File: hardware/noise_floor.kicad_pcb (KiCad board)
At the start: 2 copper layers, 51.5 x 61.6 mm, 15 parts, among them J1 DC Power, J10 IO/Switch Connector 2 (Switch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, J2 Input, J3 Output, J4 Battery Negative (optional), J5 Battery Positive (optional), J6 IO/Effect Connector 1 (IO Sid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, J7 IO/Switch Connector 1 (IO Sid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, J8 IO/Switch Connector 2 (IO Sid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, J9 IO/Switch Connector 1 (Switch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, SW1 Footswitch

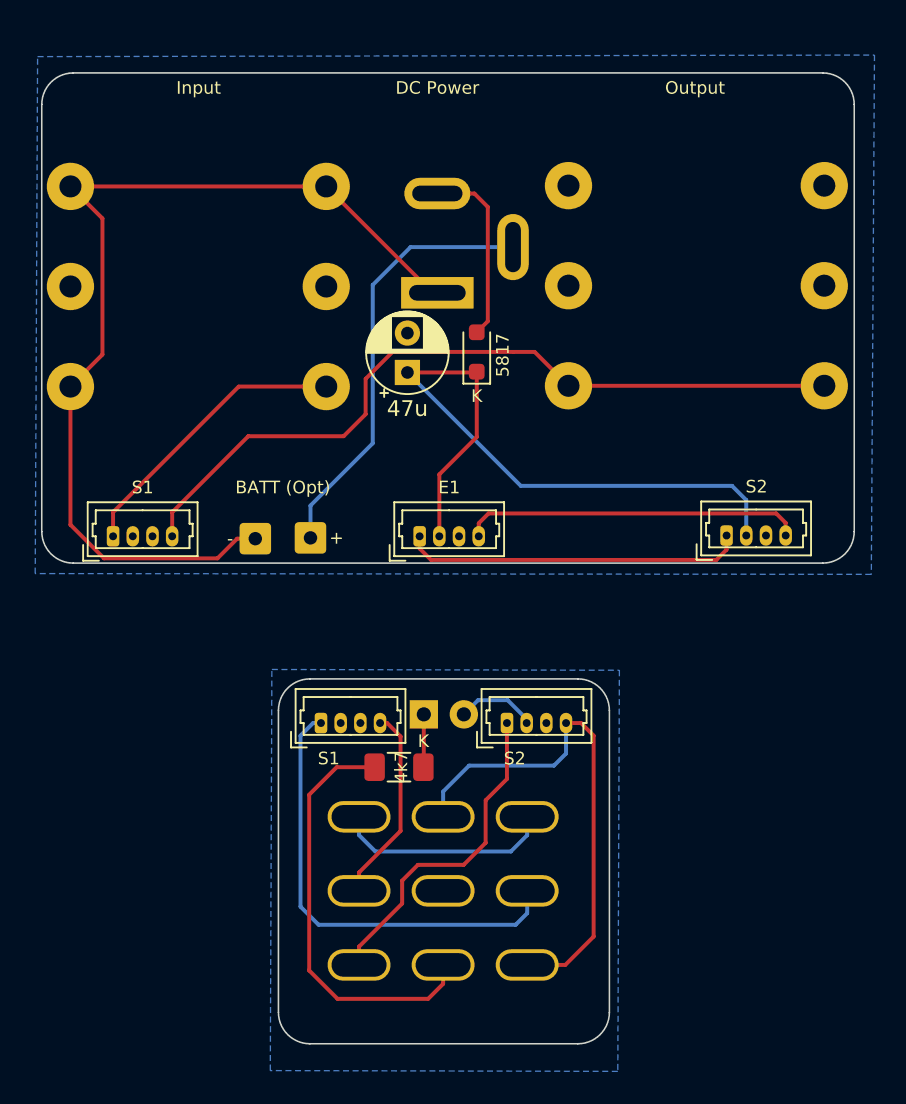
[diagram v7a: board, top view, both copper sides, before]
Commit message: Fix errata from v0.03 prototype inspection:
 - Switch to narrower amphenol phone jacks to better fit within 125B enclosure
 - Swap pin ordering for picoblade connections on IO board, as retail cable assemblies swap pin order
 -

Also:

 - Add JST XH header for battery connection

Another commit will complete the reroute shortly.
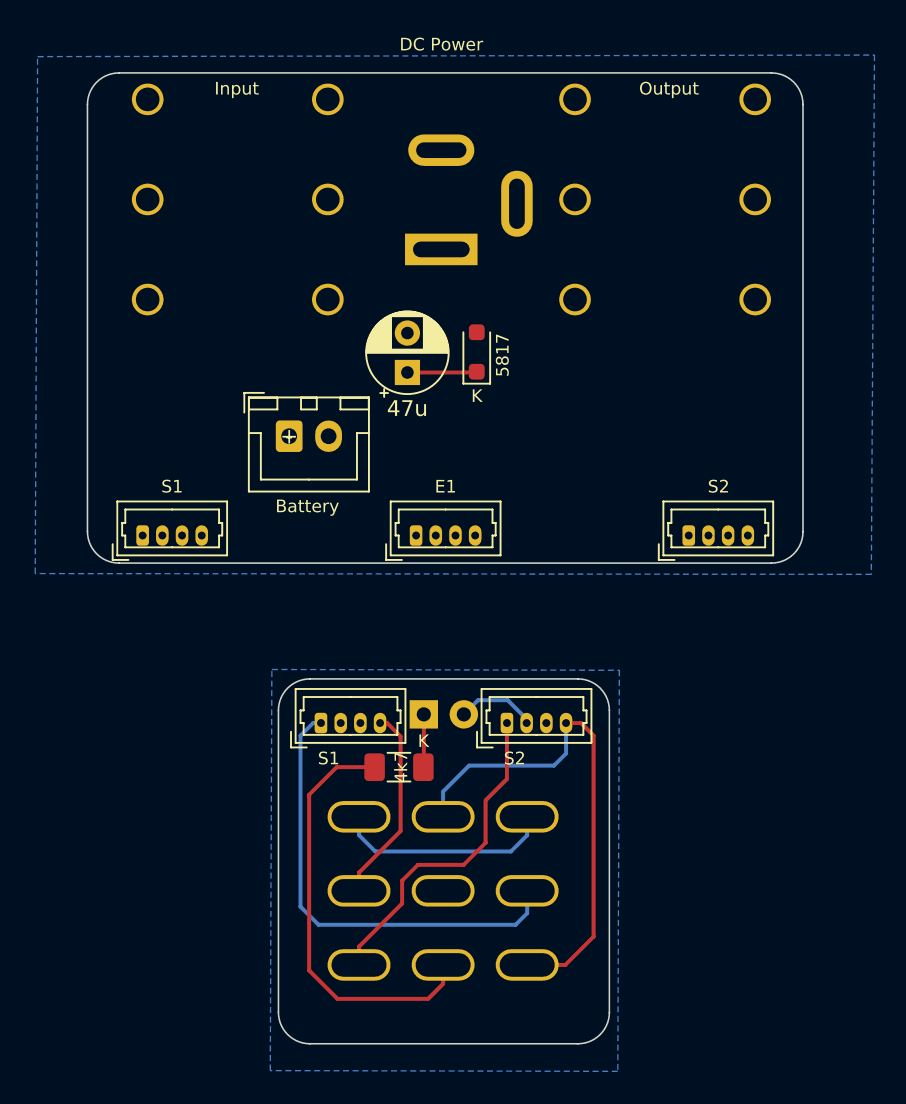
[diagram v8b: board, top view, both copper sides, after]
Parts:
- removed J4: Battery Negative (optional), Connector_Wire:SolderWire-0.25sqmm_1x01_D0.65mm_OD2mm
- removed J5: Battery Positive (optional), Connector_Wire:SolderWire-0.25sqmm_1x01_D0.65mm_OD2mm
- added J11: Battery, Connector_JST:JST_XH_B2B-XH-A_1x02_P2.50mm_Vertical, F.Cu at (31.2, 39.5)
- J2, J3: footprint noise_floor:Jack_6.35mm_Neutrik_NMJ6HCD2_Horizontal-3DModel_from_Vasily_Kashirin -> noise_floor:ACJS-MHOM
- moved J3 24.1 mm to (49.4, 18.1), turned to 0 degrees
- moved J2 21.5 mm to (22.3, 18.1), turned to 0 degrees
- moved J1 2.76 mm to (40.9, 27.6)
- moved J8 2.40 mm to (56.6, 45.8)
- moved J7 1.88 mm to (21.9, 45.8)
- moved J6 0.23 mm to (39.3, 45.8)
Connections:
- J6 pad 1: /EFFECT_OUTPUT_IO -> /EFFECT_INPUT_IO
- J6 pad 2: /9V0_IO -> GND
- J6 pad 3: GND -> /9V0_IO
- J6 pad 4: /EFFECT_INPUT_IO -> /EFFECT_OUTPUT_IO
- J7 pad 1: /INPUT_TIP_IO -> /OUTPUT_TIP_IO
- J7 pad 4: /OUTPUT_TIP_IO -> /INPUT_TIP_IO
- J8 pad 1: /EFFECT_OUTPUT_IO -> /EFFECT_INPUT_IO
- J8 pad 2: /9V0_IO -> GND
- J8 pad 3: GND -> /9V0_IO
- J8 pad 4: /EFFECT_INPUT_IO -> /EFFECT_OUTPUT_IO
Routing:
- net /BATTERY_NEG: track 62.4 -> 0.00 mm
- net /OUTPUT_TIP_IO: track 49.3 -> 0.00 mm
- net /9V0_IO: track 42.9 -> 4.35 mm
- net /BATTERY_POS: track 27.6 -> 0.00 mm
- net /EFFECT_OUTPUT_IO: track 21.7 -> 0.00 mm
- net /EFFECT_INPUT_IO: track 21.3 -> 0.00 mm
- net /INPUT_TIP_IO: track 18.4 -> 0.00 mm
- net /DC_SHIELD: track 11.8 -> 0.00 mm
- net GND: track 0.57 -> 0.00 mm
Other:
- board size 51.5 x 61.6 mm -> 45.4 x 61.6 mm
